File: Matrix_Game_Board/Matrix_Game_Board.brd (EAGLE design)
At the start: 162 x 64 mm, 53 parts, among them J1 AVR_SPI_PRG_6NS, J2 AVR_SPI_PRG_6NS, J3 AVR_SPI_PRG_6NS, J4 AVR_SPI_PRG_6NS

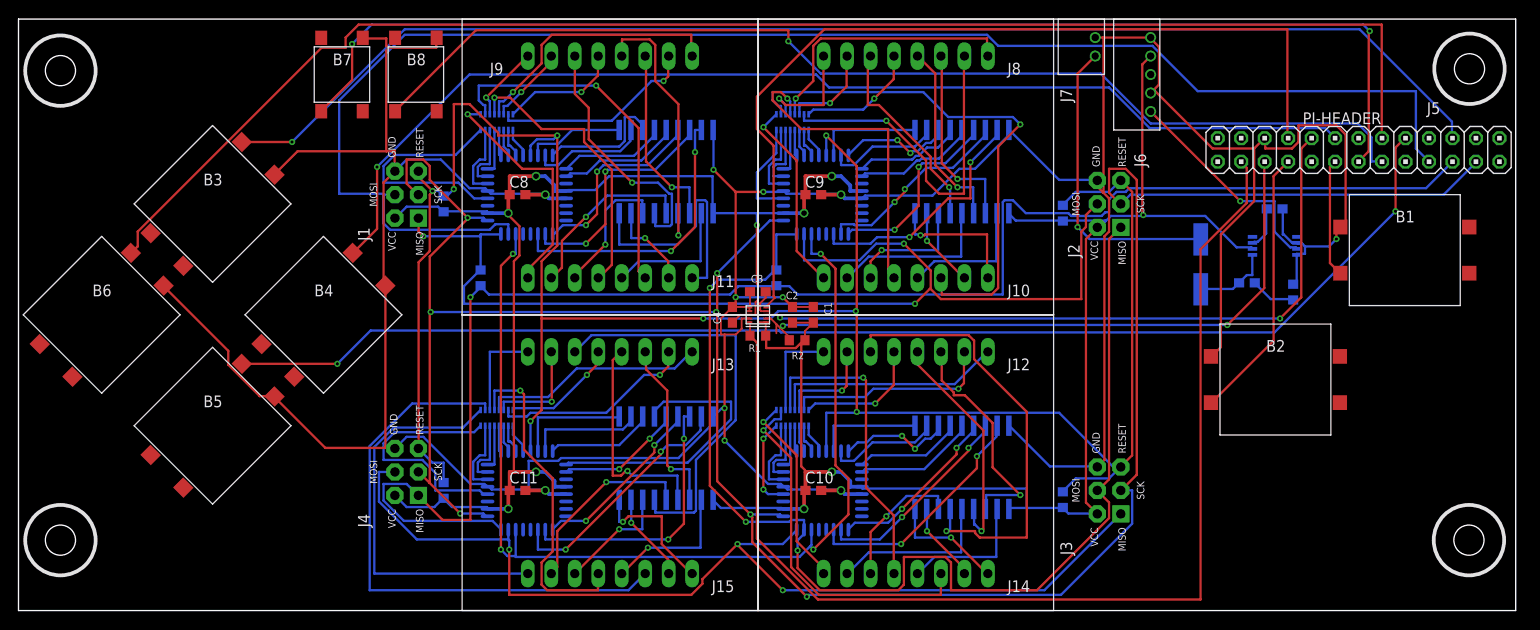
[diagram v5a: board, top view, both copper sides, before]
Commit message: Changed to right angle headers for power and speaker
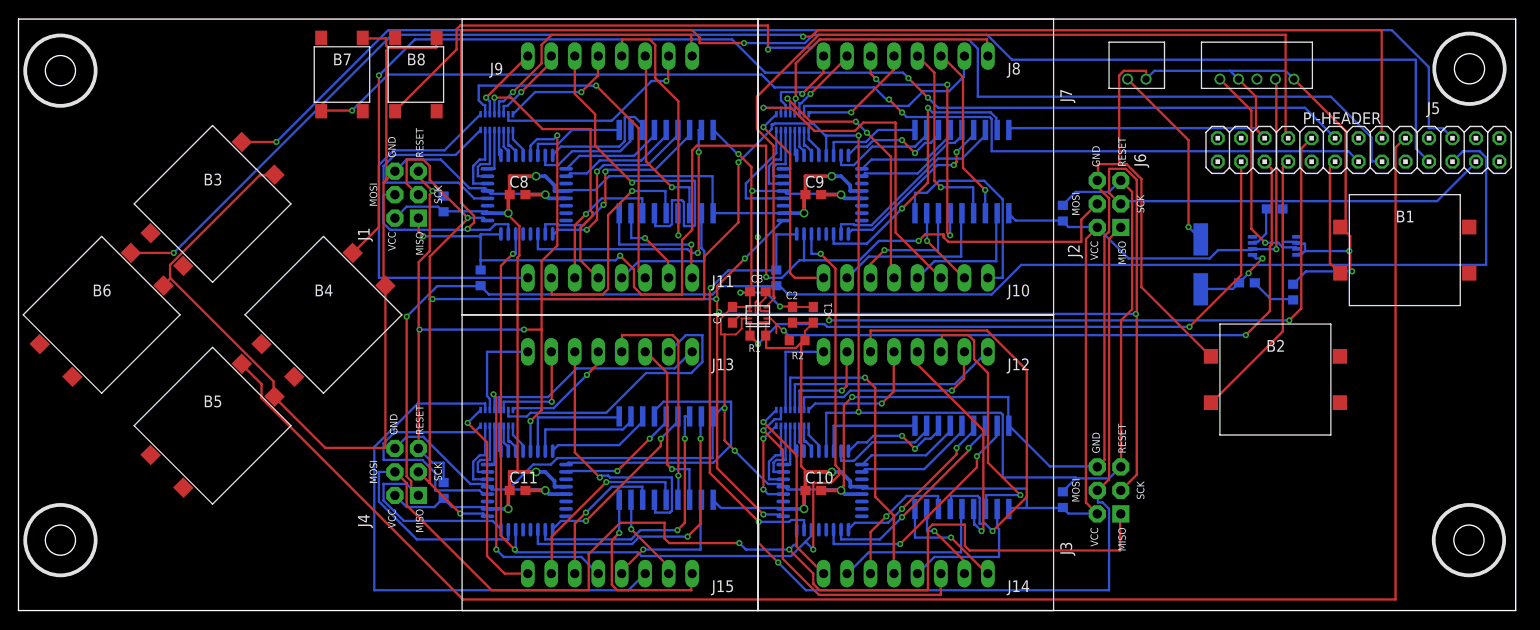
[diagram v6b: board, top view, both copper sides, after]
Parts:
- moved U$30 13.0 mm to (132.0, 59.0), turned to 0 degrees
- moved U$29 6.32 mm to (119.0, 59.0), turned to 0 degrees
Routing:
- net SDA: track 124.2 -> 70.7 mm, vias 0 -> 2
- net DOWN: track 140.2 -> 186.7 mm, vias 2 -> 0
- net GND: track 448.3 -> 484.7 mm, vias 11 -> 13
- net MISO3/MOSI4: track 109.1 -> 132.8 mm, vias 3 -> 2
- net N$51: track 58.2 -> 37.1 mm
- net N$85: track 43.5 -> 22.4 mm, vias 0 -> 1
- net N$46: track 37.5 -> 21.8 mm, vias 1 -> 0
- net N$16: track 26.0 -> 41.6 mm, vias 1 -> 0
- net N$73: track 44.8 -> 29.6 mm, vias 0 -> 1
- net START: track 134.5 -> 119.9 mm, vias 2 -> 3
- net SPK: track 33.2 -> 20.6 mm
- net N$1: track 26.4 -> 14.9 mm, vias 0 -> 1
- net N$4: track 27.7 -> 39.1 mm
- net SCK: track 265.8 -> 255.0 mm, vias 7 -> 8
- net N$79: track 21.9 -> 31.4 mm, vias 1 -> 0
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
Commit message: Inverted bottom row of matrices, routed CS, added ground plane
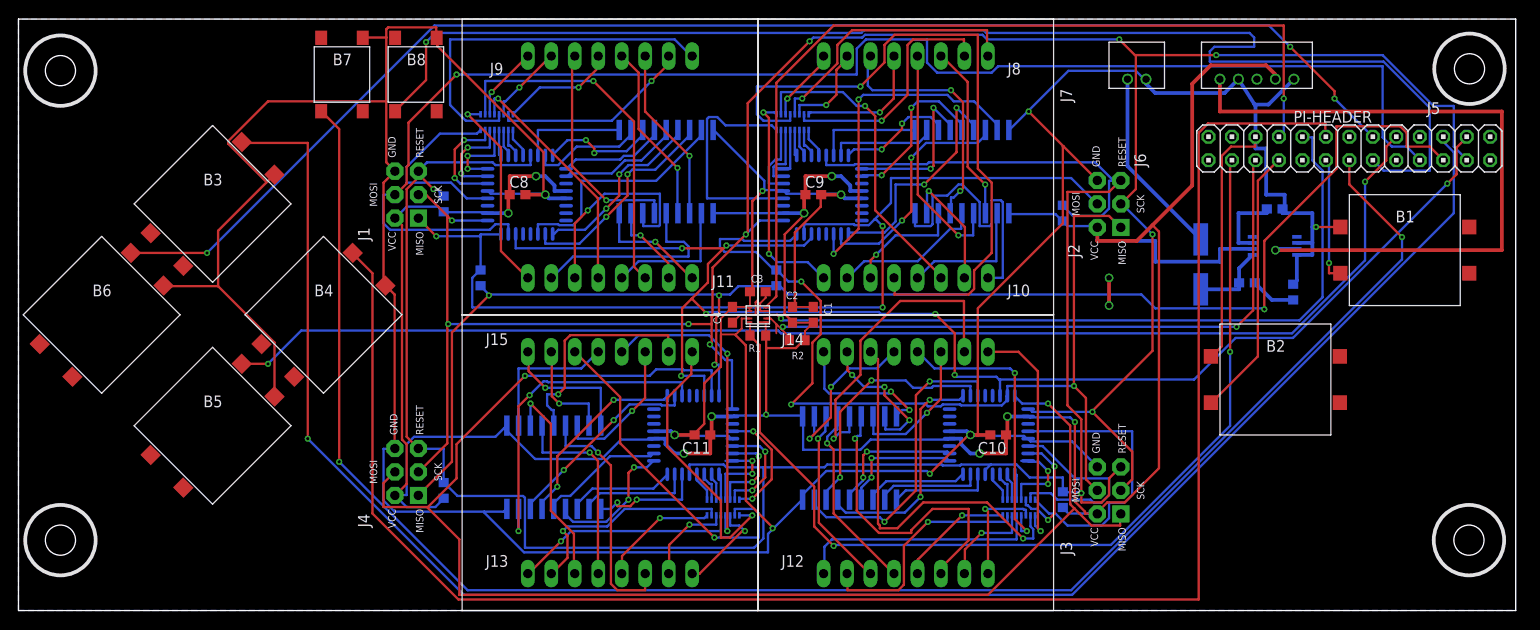
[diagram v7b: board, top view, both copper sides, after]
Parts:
- moved U$12 29.1 mm to (76.0, 12.0), turned to 270 degrees
- moved U$16 29.1 mm to (108.0, 12.0), turned to 270 degrees
- moved C10 20.9 mm to (104.0, 19.0), turned to 180 degrees
- moved C11 20.9 mm to (72.0, 19.0), turned to 180 degrees
- moved U$11 19.0 mm to (71.0, 19.0), turned to 180 degrees
- moved U$15 19.0 mm to (103.0, 19.0), turned to 180 degrees
- moved U$10 10.2 mm to (61.0, 11.0), turned to 0 degrees
- moved U$14 8.25 mm to (93.0, 12.0), turned to 0 degrees
- moved PI-HEADER 1.01 mm to (142.0, 50.0)
- turned U$13 to 180 degrees
- turned U$8 to 180 degrees
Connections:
- net SS: now also PI-HEADER.24
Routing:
- net START: track 119.9 -> 187.4 mm, vias 3 -> 2
- net RIGHT: track 129.9 -> 188.4 mm, vias 3 -> 0
- net AUDIO: track 23.4 -> 76.0 mm
- net UP: track 144.7 -> 196.0 mm
- net SS: track 111.3 -> 159.5 mm, vias 4 -> 7
- net N$49: track 28.9 -> 74.5 mm, vias 3 -> 1
- net DOWN: track 186.7 -> 141.2 mm, vias 0 -> 2
- net VCC: track 296.1 -> 340.3 mm
- net SDA: track 70.7 -> 105.1 mm
- net MISO2/MOSI3: track 131.4 -> 104.8 mm
- net MISO3/MOSI4: track 132.8 -> 155.8 mm
- net N$84: track 60.2 -> 37.3 mm, vias 0 -> 1
- net N$102: track 9.84 -> 32.2 mm, vias 2 -> 0
- net GND: track 484.7 -> 506.4 mm, vias 13 -> 11
- net SELECT: track 125.0 -> 145.7 mm
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- added copper zone on layer 16, net GND

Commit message: Moved buttons down, moved large capacitor to top of board
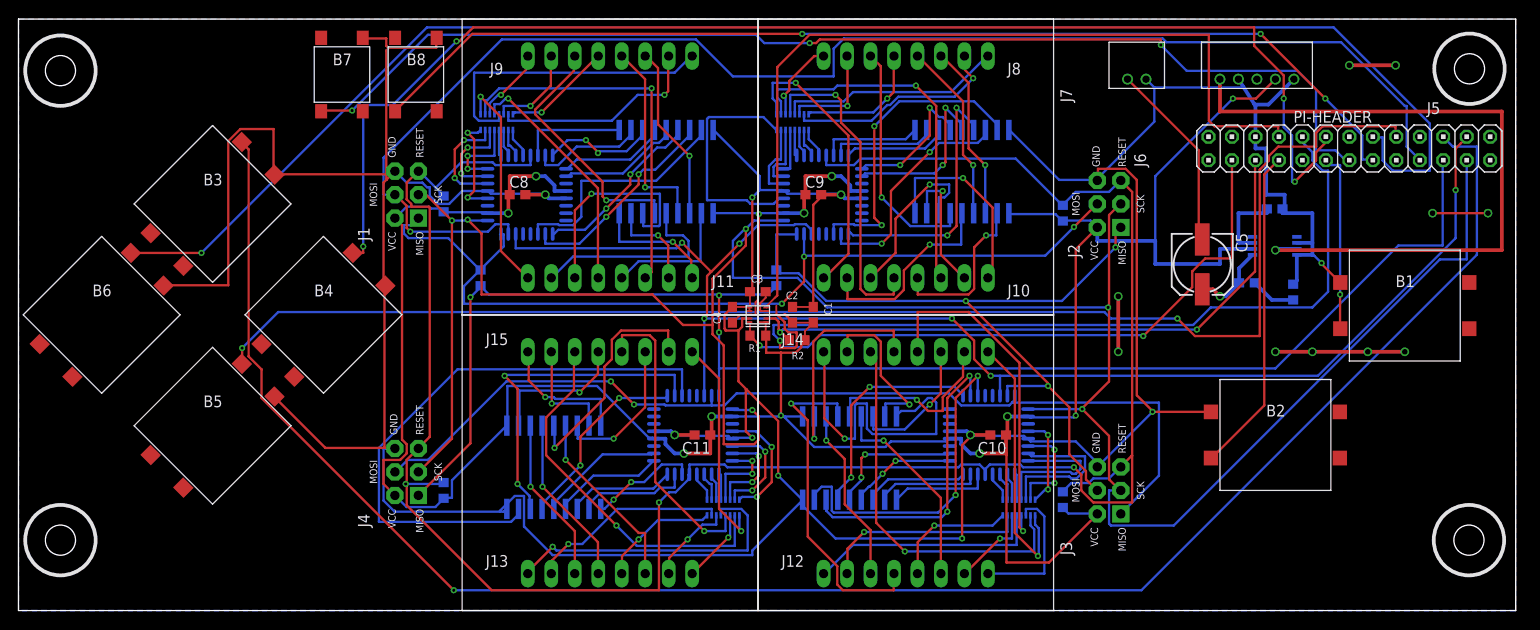
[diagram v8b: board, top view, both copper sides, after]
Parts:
- moved U$21 6.00 mm to (148.0, 33.0)
- moved U$22 6.00 mm to (134.0, 19.0)
- moved C5 0.16 mm to (126.1, 37.5), flipped to the top
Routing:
- net START: track 187.4 -> 124.9 mm, vias 2 -> 3
- net MISO3/MOSI4: track 155.8 -> 104.7 mm
- net RIGHT: track 188.4 -> 142.0 mm, vias 0 -> 4
- net N$49: track 74.5 -> 34.8 mm
- net SDA: track 105.1 -> 69.8 mm
- net SELECT: track 145.7 -> 116.5 mm, vias 1 -> 3
- net N$93: track 36.2 -> 63.2 mm, vias 2 -> 0
- net MISO2/MOSI3: track 104.8 -> 80.8 mm
- net N$102: track 32.2 -> 10.1 mm, vias 0 -> 2
- net N$103: track 16.1 -> 35.7 mm, vias 2 -> 1
- net LEFT: track 150.0 -> 169.2 mm, vias 3 -> 1
- net VCC: track 340.3 -> 321.8 mm, vias 10 -> 12
- net N$108: track 20.7 -> 36.3 mm
- net N$92: track 21.7 -> 36.3 mm
- net N$107: track 34.0 -> 20.0 mm
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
